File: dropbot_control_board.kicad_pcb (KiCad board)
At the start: 4 copper layers, 115 x 92 mm, 139 parts, among them IC1 MCP6024, J1 TFM-105-02-X-DH, P1 CONN_01X01, P10 CONN_01X01, P2 CONN_01X01, P3 CONN_01X04, P4 CONN_01X04, P5 CONN_01X01, P6 USB_B, P7 CONN_01X04, P8 CONN_01X03, P9 USB_A, Q1 STP33N65M2, Q5 IRF740BPBF, Q6 IRF740BPBF, SW1 PROG, U1 Teensy_3.2, U10 W25Q64FV, U2 MAX1771, U3 CAT5171, U4 HV7802, U5 DPST (2 Form A), 350V, U6 NCP5304, U7 DPST (2 Form A), 350V, U8 DPST (2 Form A), 350V, U9 74AHC1G32

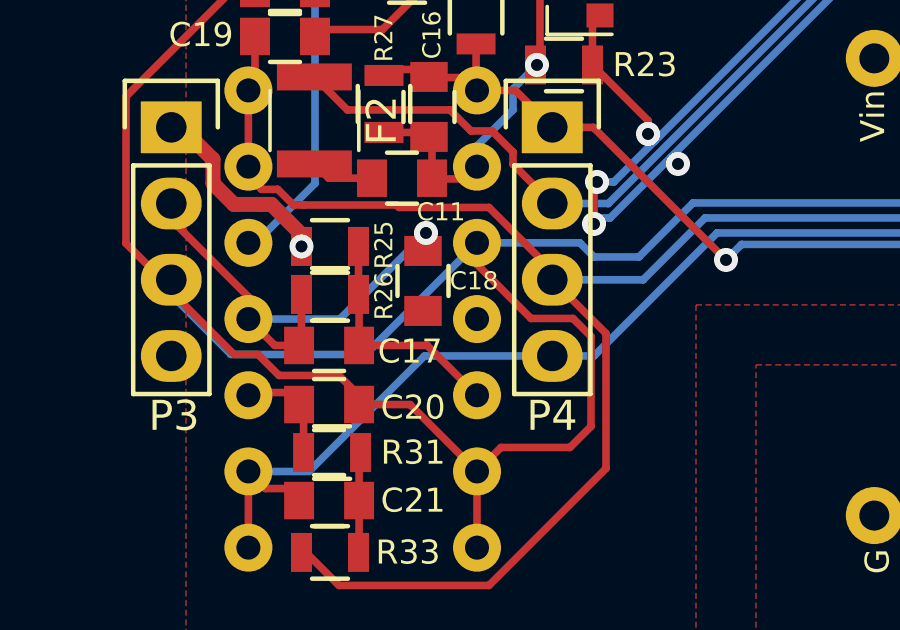
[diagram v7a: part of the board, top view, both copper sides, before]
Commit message: [WIP] Fixes #1: C18 is disconnected
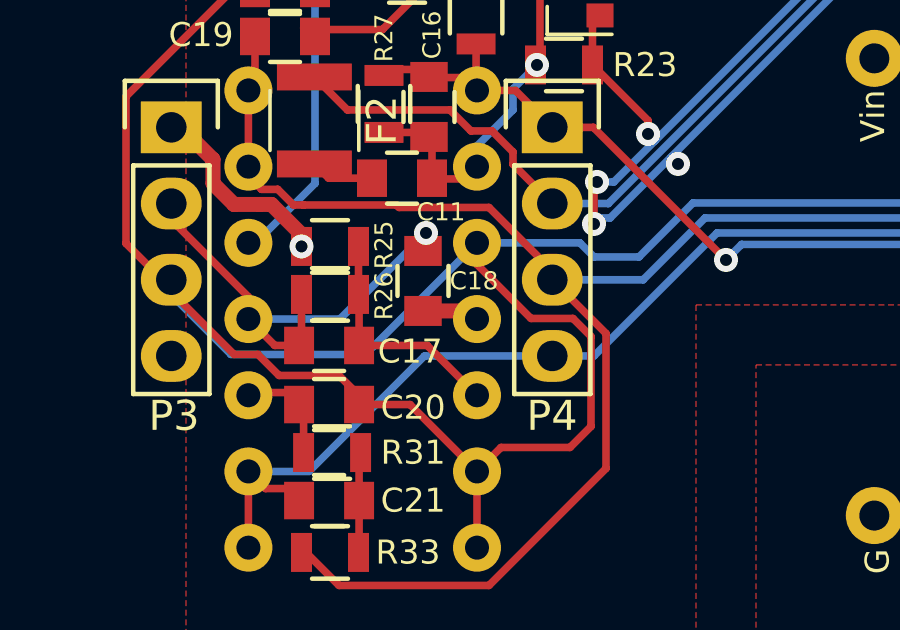
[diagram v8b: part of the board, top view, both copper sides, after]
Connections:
- C18 pad 1: Net-(C18-Pad1) -> +3.3V
- SW1 pad 3: (no net) -> CHASIS_GND
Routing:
- net +3.3V: track 99.8 -> 101.7 mm
- net (no net): track 84.5 -> 83.8 mm, vias 13 -> 12
- net CHASIS_GND: track 11.7 -> 12.4 mm, vias 9 -> 10
